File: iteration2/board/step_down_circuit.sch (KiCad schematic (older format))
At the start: 6 parts

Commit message: Redo netlist
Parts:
- C2: renamed from C?; footprint ~ -> Capacitors_SMD:C_0805_HandSoldering
- D1: renamed from D?; footprint ~ -> Diodes_SMD:D_0805
- Q1: renamed from Q?; footprint ~ -> TO_SOT_Packages_SMD:SOT-23
- R1, R2, R3: renamed from R?; footprint ~ -> Resistors_SMD:R_0805_HandSoldering
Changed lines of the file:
@@
 $EndDescr
 $Comp
-L C C?
+L C C2
 U 1 1 59EC7CB5
 P 5200 4500
-F 0 "C?" H 5200 4600 40  0000 L CNN
+AR Path="/59EC784F/59EC7CB5" Ref="C2"  Part="1"
+AR Path="/59EC8586/59EC7CB5" Ref="C3"  Part="1"
+AR Path="/59EC8F0E/59EC7CB5" Ref="C4"  Part="1"
+F 0 "C2" H 5200 4600 40  0000 L CNN
 F 1 "100nF" H 5206 4415 40  0000 L CNN
-F 2 "~" H 5238 4350 30  0000 C CNN
+F 2 "Capacitors_SMD:C_0805_HandSoldering" H 5238 4350 30  0000 C CNN
 F 3 "~" H 5200 4500 60  0000 C CNN
 	1    5200 4500
@@
 $EndComp
 $Comp
-L R R?
+L R R1
 U 1 1 59EC7CBC
 P 5200 4050
-F 0 "R?" V 5280 4050 40  0000 C CNN
+AR Path="/59EC784F/59EC7CBC" Ref="R1"  Part="1"
+AR Path="/59EC8586/59EC7CBC" Ref="R4"  Part="1"
+AR Path="/59EC8F0E/59EC7CBC" Ref="R7"  Part="1"
+F 0 "R1" V 5280 4050 40  0000 C CNN
 F 1 "10K" V 5207 4051 40  0000 C CNN
-F 2 "~" V 5130 4050 30  0000 C CNN
+F 2 "Resistors_SMD:R_0805_HandSoldering" V 5130 4050 30  0000 C CNN
 F 3 "~" H 5200 4050 30  0000 C CNN
 	1    5200 4050
@@
 $EndComp
 $Comp
-L R R?
+L R R2
 U 1 1 59EC7CC3
 P 5450 4300
-F 0 "R?" V 5530 4300 40  0000 C CNN
+AR Path="/59EC784F/59EC7CC3" Ref="R2"  Part="1"
+AR Path="/59EC8586/59EC7CC3" Ref="R5"  Part="1"
+AR Path="/59EC8F0E/59EC7CC3" Ref="R8"  Part="1"
+F 0 "R2" V 5530 4300 40  0000 C CNN
 F 1 "10K" V 5457 4301 40  0000 C CNN
-F 2 "~" V 5380 4300 30  0000 C CNN
+F 2 "Resistors_SMD:R_0805_HandSoldering" V 5380 4300 30  0000 C CNN
 F 3 "~" H 5450 4300 30  0000 C CNN
 	1    5450 4300
@@
 +12V
 $Comp
-L GND #PWR?
+L GND #PWR7
 U 1 1 59EC7CCB
 P 5200 4700
-F 0 "#PWR?" H 5200 4700 30  0001 C CNN
+AR Path="/59EC784F/59EC7CCB" Ref="#PWR7"  Part="1"
+AR Path="/59EC8586/59EC7CCB" Ref="#PWR10"  Part="1"
+AR Path="/59EC8F0E/59EC7CCB" Ref="#PWR13"  Part="1"
+F 0 "#PWR7" H 5200 4700 30  0001 C CNN
 F 1 "GND" H 5200 4630 30  0001 C CNN
 F 2 "" H 5200 4700 60  0000 C CNN
@@
 $EndComp
 $Comp
-L MOS_N Q?
+L MOS_N Q1
 U 1 1 59EC7CD1
 P 6250 4300
-F 0 "Q?" H 6260 4470 60  0000 R CNN
+AR Path="/59EC784F/59EC7CD1" Ref="Q1"  Part="1"
+AR Path="/59EC8586/59EC7CD1" Ref="Q2"  Part="1"
+AR Path="/59EC8F0E/59EC7CD1" Ref="Q3"  Part="1"
+F 0 "Q1" H 6260 4470 60  0000 R CNN
 F 1 "2N7002" H 6260 4150 60  0000 R CNN
-F 2 "~" H 6250 4300 60  0000 C CNN
+F 2 "TO_SOT_Packages_SMD:SOT-23" H 6250 4300 60  0000 C CNN
 F 3 "~" H 6250 4300 60  0000 C CNN
 	1    6250 4300
@@
 $EndComp
 $Comp
-L R R?
+L R R3
 U 1 1 59EC7CD8
 P 6350 3850
-F 0 "R?" V 6430 3850 40  0000 C CNN
+AR Path="/59EC784F/59EC7CD8" Ref="R3"  Part="1"
+AR Path="/59EC8586/59EC7CD8" Ref="R6"  Part="1"
+AR Path="/59EC8F0E/59EC7CD8" Ref="R9"  Part="1"
+F 0 "R3" V 6430 3850 40  0000 C CNN
 F 1 "10K" V 6357 3851 40  0000 C CNN
-F 2 "~" V 6280 3850 30  0000 C CNN
+F 2 "Resistors_SMD:R_0805_HandSoldering" V 6280 3850 30  0000 C CNN
 F 3 "~" H 6350 3850 30  0000 C CNN
 	1    6350 3850
@@
 $EndComp
 $Comp
-L GND #PWR?
+L GND #PWR9
 U 1 1 59EC7CDF
 P 6350 4500
-F 0 "#PWR?" H 6350 4500 30  0001 C CNN
+AR Path="/59EC784F/59EC7CDF" Ref="#PWR9"  Part="1"
+AR Path="/59EC8586/59EC7CDF" Ref="#PWR12"  Part="1"
+AR Path="/59EC8F0E/59EC7CDF" Ref="#PWR15"  Part="1"
+F 0 "#PWR9" H 6350 4500 30  0001 C CNN
 F 1 "GND" H 6350 4430 30  0001 C CNN
 F 2 "" H 6350 4500 60  0000 C CNN
@@
 +3.3V
 $Comp
-L BAV99 D?
+L BAV99 D1
 U 1 1 59EC7CE6
 P 5800 4350
-F 0 "D?" H 5900 4300 40  0000 C CNN
+AR Path="/59EC784F/59EC7CE6" Ref="D1"  Part="1"
+AR Path="/59EC8586/59EC7CE6" Ref="D2"  Part="1"
+AR Path="/59EC8F0E/59EC7CE6" Ref="D3"  Part="1"
+F 0 "D1" H 5900 4300 40  0000 C CNN
 F 1 "BAV99" H 5900 4400 40  0001 C CNN
-F 2 "~" V 5850 4300 60  0000 C CNN
+F 2 "Diodes_SMD:D_0805" V 5850 4300 60  0000 C CNN
 F 3 "~" V 5850 4300 60  0000 C CNN
 	1    5800 4350
@@
 	5700 4600 5700 4300
 $Comp
-L GND #PWR?
+L GND #PWR8
 U 1 1 59EC7CF0
 P 5800 4500
-F 0 "#PWR?" H 5800 4500 30  0001 C CNN
+AR Path="/59EC784F/59EC7CF0" Ref="#PWR8"  Part="1"
+AR Path="/59EC8586/59EC7CF0" Ref="#PWR11"  Part="1"
+AR Path="/59EC8F0E/59EC7CF0" Ref="#PWR14"  Part="1"
+F 0 "#PWR8" H 5800 4500 30  0001 C CNN
 F 1 "GND" H 5800 4430 30  0001 C CNN
 F 2 "" H 5800 4500 60  0000 C CNN

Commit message: Generated netlist
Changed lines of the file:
@@
 AR Path="/59EC8586/59EC7CB5" Ref="C3"  Part="1"
 AR Path="/59EC8F0E/59EC7CB5" Ref="C4"  Part="1"
-F 0 "C2" H 5200 4600 40  0000 L CNN
+F 0 "C4" H 5200 4600 40  0000 L CNN
 F 1 "100nF" H 5206 4415 40  0000 L CNN
 F 2 "Capacitors_SMD:C_0805_HandSoldering" H 5238 4350 30  0000 C CNN
@@
 AR Path="/59EC8586/59EC7CBC" Ref="R4"  Part="1"
 AR Path="/59EC8F0E/59EC7CBC" Ref="R7"  Part="1"
-F 0 "R1" V 5280 4050 40  0000 C CNN
+F 0 "R7" V 5280 4050 40  0000 C CNN
 F 1 "10K" V 5207 4051 40  0000 C CNN
 F 2 "Resistors_SMD:R_0805_HandSoldering" V 5130 4050 30  0000 C CNN
@@
 AR Path="/59EC8586/59EC7CC3" Ref="R5"  Part="1"
 AR Path="/59EC8F0E/59EC7CC3" Ref="R8"  Part="1"
-F 0 "R2" V 5530 4300 40  0000 C CNN
+F 0 "R8" V 5530 4300 40  0000 C CNN
 F 1 "10K" V 5457 4301 40  0000 C CNN
 F 2 "Resistors_SMD:R_0805_HandSoldering" V 5380 4300 30  0000 C CNN
@@
 AR Path="/59EC8586/59EC7CD1" Ref="Q2"  Part="1"
 AR Path="/59EC8F0E/59EC7CD1" Ref="Q3"  Part="1"
-F 0 "Q1" H 6260 4470 60  0000 R CNN
+F 0 "Q3" H 6260 4470 60  0000 R CNN
 F 1 "2N7002" H 6260 4150 60  0000 R CNN
 F 2 "TO_SOT_Packages_SMD:SOT-23" H 6250 4300 60  0000 C CNN
@@
 AR Path="/59EC8586/59EC7CD8" Ref="R6"  Part="1"
 AR Path="/59EC8F0E/59EC7CD8" Ref="R9"  Part="1"
-F 0 "R3" V 6430 3850 40  0000 C CNN
+F 0 "R9" V 6430 3850 40  0000 C CNN
 F 1 "10K" V 6357 3851 40  0000 C CNN
 F 2 "Resistors_SMD:R_0805_HandSoldering" V 6280 3850 30  0000 C CNN
@@
 AR Path="/59EC8586/59EC7CE6" Ref="D2"  Part="1"
 AR Path="/59EC8F0E/59EC7CE6" Ref="D3"  Part="1"
-F 0 "D1" H 5900 4300 40  0000 C CNN
+F 0 "D3" H 5900 4300 40  0000 C CNN
 F 1 "BAV99" H 5900 4400 40  0001 C CNN
 F 2 "Diodes_SMD:D_0805" V 5850 4300 60  0000 C CNN

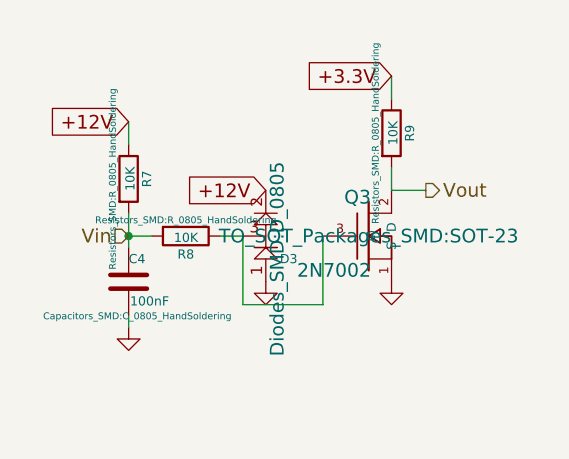
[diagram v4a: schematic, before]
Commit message: Redid some components to fit footprint
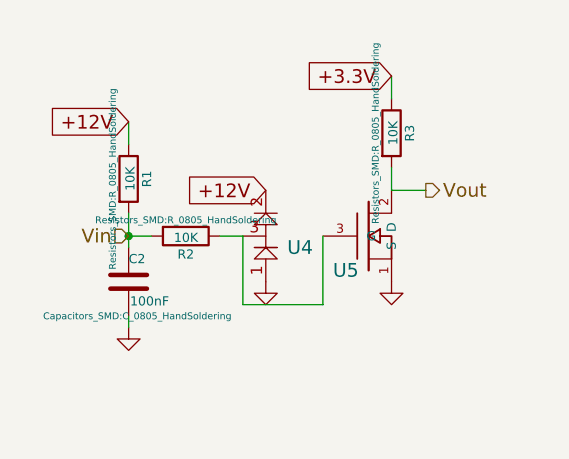
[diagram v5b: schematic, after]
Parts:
- removed D1: BAV99, Diodes_SMD:D_0805, symbol BAV99
- removed Q1: 2N7002, TO_SOT_Packages_SMD:SOT-23, symbol MOS_N
- added U7: MOS_N, TO_SOT_Packages_SMD:SOT-23, symbol MOS_N
- added U8: BAV99, TO_SOT_Packages_SMD:SOT-23, symbol BAV99
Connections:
- net +12V: now also U8.2
- net GND: now also U7.1 (S), U8.1
- net Vout: now also U7.2 (D)
- net at R2.1: now also U7.3 (G), U8.3
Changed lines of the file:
@@
 $Descr A4 11693 8268
 encoding utf-8
-Sheet 2 5
+Sheet 3 5
 Title ""
 Date ""
@@
 AR Path="/59EC8586/59EC7CB5" Ref="C3"  Part="1"
 AR Path="/59EC8F0E/59EC7CB5" Ref="C4"  Part="1"
-F 0 "C4" H 5200 4600 40  0000 L CNN
+F 0 "C2" H 5200 4600 40  0000 L CNN
 F 1 "100nF" H 5206 4415 40  0000 L CNN
 F 2 "Capacitors_SMD:C_0805_HandSoldering" H 5238 4350 30  0000 C CNN
@@
 AR Path="/59EC8586/59EC7CBC" Ref="R4"  Part="1"
 AR Path="/59EC8F0E/59EC7CBC" Ref="R7"  Part="1"
-F 0 "R7" V 5280 4050 40  0000 C CNN
+F 0 "R1" V 5280 4050 40  0000 C CNN
 F 1 "10K" V 5207 4051 40  0000 C CNN
 F 2 "Resistors_SMD:R_0805_HandSoldering" V 5130 4050 30  0000 C CNN
@@
 AR Path="/59EC8586/59EC7CC3" Ref="R5"  Part="1"
 AR Path="/59EC8F0E/59EC7CC3" Ref="R8"  Part="1"
-F 0 "R8" V 5530 4300 40  0000 C CNN
+F 0 "R2" V 5530 4300 40  0000 C CNN
 F 1 "10K" V 5457 4301 40  0000 C CNN
 F 2 "Resistors_SMD:R_0805_HandSoldering" V 5380 4300 30  0000 C CNN
@@
 $EndComp
 $Comp
-L MOS_N Q1
-U 1 1 59EC7CD1
-P 6250 4300
-AR Path="/59EC784F/59EC7CD1" Ref="Q1"  Part="1"
-AR Path="/59EC8586/59EC7CD1" Ref="Q2"  Part="1"
-AR Path="/59EC8F0E/59EC7CD1" Ref="Q3"  Part="1"
-F 0 "Q3" H 6260 4470 60  0000 R CNN
-F 1 "2N7002" H 6260 4150 60  0000 R CNN
-F 2 "TO_SOT_Packages_SMD:SOT-23" H 6250 4300 60  0000 C CNN
-F 3 "~" H 6250 4300 60  0000 C CNN
-	1    6250 4300
-	1    0    0    -1
-$EndComp
-$Comp
 L R R3
 U 1 1 59EC7CD8
@@
 AR Path="/59EC8586/59EC7CD8" Ref="R6"  Part="1"
 AR Path="/59EC8F0E/59EC7CD8" Ref="R9"  Part="1"
-F 0 "R9" V 6430 3850 40  0000 C CNN
+F 0 "R3" V 6430 3850 40  0000 C CNN
 F 1 "10K" V 6357 3851 40  0000 C CNN
 F 2 "Resistors_SMD:R_0805_HandSoldering" V 6280 3850 30  0000 C CNN
@@
 Text GLabel 6350 3600 0    60   Input ~ 0
 +3.3V
-$Comp
-L BAV99 D1
-U 1 1 59EC7CE6
-P 5800 4350
-AR Path="/59EC784F/59EC7CE6" Ref="D1"  Part="1"
-AR Path="/59EC8586/59EC7CE6" Ref="D2"  Part="1"
-AR Path="/59EC8F0E/59EC7CE6" Ref="D3"  Part="1"
-F 0 "D3" H 5900 4300 40  0000 C CNN
-F 1 "BAV99" H 5900 4400 40  0001 C CNN
-F 2 "Diodes_SMD:D_0805" V 5850 4300 60  0000 C CNN
-F 3 "~" V 5850 4300 60  0000 C CNN
-	1    5800 4350
-	1    0    0    -1
-$EndComp
 Wire Wire Line
 	6050 4300 6050 4600
@@
 Text HLabel 6500 4100 2    60   Output ~ 0
 Vout
+$Comp
+L BAV99 U8
+U 1 1 59F295CD
+P 5800 4350
+AR Path="/59EC8F0E/59F295CD" Ref="U8"  Part="1"
+AR Path="/59EC8586/59F295CD" Ref="U6"  Part="1"
+AR Path="/59EC784F/59F295CD" Ref="U4"  Part="1"
+F 0 "U4" H 5950 4350 60  0000 C CNN
+F 1 "BAV99" H 6050 4450 60  0001 C CNN
+F 2 "TO_SOT_Packages_SMD:SOT-23" H 5800 4350 60  0001 C CNN
+F 3 "" H 5800 4350 60  0001 C CNN
+	1    5800 4350
+	1    0    0    -1
+$EndComp
+$Comp
+L MOS_N U7
+U 1 1 59F29BA9
+P 6250 4300
+AR Path="/59EC8586/59F29BA9" Ref="U7"  Part="1"
+AR Path="/59EC784F/59F29BA9" Ref="U5"  Part="1"
+AR Path="/59EC8F0E/59F29BA9" Ref="U9"  Part="1"
+F 0 "U5" H 6150 4150 60  0000 C CNN
+F 1 "MOS_N" H 6550 4350 60  0001 C CNN
+F 2 "TO_SOT_Packages_SMD:SOT-23" H 6250 4300 60  0001 C CNN
+F 3 "" H 6250 4300 60  0001 C CNN
+	1    6250 4300
+	1    0    0    -1
+$EndComp
 $EndSCHEMATC

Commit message: partially resolved merge issues and added script for automatic merging
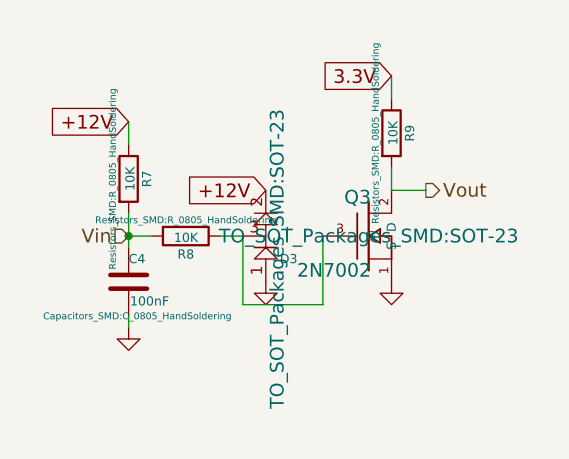
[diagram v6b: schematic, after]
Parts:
- removed U7: MOS_N, TO_SOT_Packages_SMD:SOT-23, symbol MOS_N
- removed U8: BAV99, TO_SOT_Packages_SMD:SOT-23, symbol BAV99
- added D2: BAV99, TO_SOT_Packages_SMD:SOT-23, symbol BAV99
- added Q2: 2N7002, TO_SOT_Packages_SMD:SOT-23, symbol MOS_N
- renumbered C2 to C3, R1 to R4, R2 to R5, R3 to R6
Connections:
- net +12V: now also D2.2
- net GND: now also D2.1, Q2.1 (S)
- net Vout: now also Q2.2 (D)
- net at R5.1: now also D2.3, Q2.3 (G)
- net +3.3V renamed 3.3V
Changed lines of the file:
@@
 $Descr A4 11693 8268
 encoding utf-8
-Sheet 3 5
+Sheet 4 5
 Title ""
 Date ""
@@
 $EndDescr
 $Comp
-L C C2
+L C C3
 U 1 1 59EC7CB5
 P 5200 4500
-AR Path="/59EC784F/59EC7CB5" Ref="C2"  Part="1"
 AR Path="/59EC8586/59EC7CB5" Ref="C3"  Part="1"
 AR Path="/59EC8F0E/59EC7CB5" Ref="C4"  Part="1"
-F 0 "C2" H 5200 4600 40  0000 L CNN
+AR Path="/59EC784F/59EC7CB5" Ref="C2"  Part="1"
+F 0 "C4" H 5200 4600 40  0000 L CNN
 F 1 "100nF" H 5206 4415 40  0000 L CNN
 F 2 "Capacitors_SMD:C_0805_HandSoldering" H 5238 4350 30  0000 C CNN
@@
 $EndComp
 $Comp
-L R R1
+L R R4
 U 1 1 59EC7CBC
 P 5200 4050
-AR Path="/59EC784F/59EC7CBC" Ref="R1"  Part="1"
 AR Path="/59EC8586/59EC7CBC" Ref="R4"  Part="1"
 AR Path="/59EC8F0E/59EC7CBC" Ref="R7"  Part="1"
-F 0 "R1" V 5280 4050 40  0000 C CNN
+AR Path="/59EC784F/59EC7CBC" Ref="R1"  Part="1"
+F 0 "R7" V 5280 4050 40  0000 C CNN
 F 1 "10K" V 5207 4051 40  0000 C CNN
 F 2 "Resistors_SMD:R_0805_HandSoldering" V 5130 4050 30  0000 C CNN
@@
 $EndComp
 $Comp
-L R R2
+L R R5
 U 1 1 59EC7CC3
 P 5450 4300
-AR Path="/59EC784F/59EC7CC3" Ref="R2"  Part="1"
 AR Path="/59EC8586/59EC7CC3" Ref="R5"  Part="1"
 AR Path="/59EC8F0E/59EC7CC3" Ref="R8"  Part="1"
-F 0 "R2" V 5530 4300 40  0000 C CNN
+AR Path="/59EC784F/59EC7CC3" Ref="R2"  Part="1"
+F 0 "R8" V 5530 4300 40  0000 C CNN
 F 1 "10K" V 5457 4301 40  0000 C CNN
 F 2 "Resistors_SMD:R_0805_HandSoldering" V 5380 4300 30  0000 C CNN
@@
 +12V
 $Comp
-L GND #PWR07
+L GND #PWR10
 U 1 1 59EC7CCB
 P 5200 4700
-AR Path="/59EC784F/59EC7CCB" Ref="#PWR07"  Part="1"
-AR Path="/59EC8586/59EC7CCB" Ref="#PWR010"  Part="1"
-AR Path="/59EC8F0E/59EC7CCB" Ref="#PWR013"  Part="1"
-F 0 "#PWR013" H 5200 4700 30  0001 C CNN
+AR Path="/59EC8586/59EC7CCB" Ref="#PWR10"  Part="1"
+AR Path="/59EC8F0E/59EC7CCB" Ref="#PWR13"  Part="1"
+AR Path="/59EC784F/59EC7CCB" Ref="#PWR7"  Part="1"
+F 0 "#PWR13" H 5200 4700 30  0001 C CNN
 F 1 "GND" H 5200 4630 30  0001 C CNN
 F 2 "" H 5200 4700 60  0000 C CNN
@@
 $EndComp
 $Comp
-L R R3
+L MOS_N Q2
+U 1 1 59EC7CD1
+P 6250 4300
+AR Path="/59EC8586/59EC7CD1" Ref="Q2"  Part="1"
+AR Path="/59EC8F0E/59EC7CD1" Ref="Q3"  Part="1"
+AR Path="/59EC784F/59EC7CD1" Ref="Q1"  Part="1"
+F 0 "Q3" H 6260 4470 60  0000 R CNN
+F 1 "2N7002" H 6260 4150 60  0000 R CNN
+F 2 "TO_SOT_Packages_SMD:SOT-23" H 6250 4300 60  0000 C CNN
+F 3 "~" H 6250 4300 60  0000 C CNN
+	1    6250 4300
+	1    0    0    -1
+$EndComp
+$Comp
+L R R6
 U 1 1 59EC7CD8
 P 6350 3850
-AR Path="/59EC784F/59EC7CD8" Ref="R3"  Part="1"
 AR Path="/59EC8586/59EC7CD8" Ref="R6"  Part="1"
 AR Path="/59EC8F0E/59EC7CD8" Ref="R9"  Part="1"
-F 0 "R3" V 6430 3850 40  0000 C CNN
+AR Path="/59EC784F/59EC7CD8" Ref="R3"  Part="1"
+F 0 "R9" V 6430 3850 40  0000 C CNN
 F 1 "10K" V 6357 3851 40  0000 C CNN
 F 2 "Resistors_SMD:R_0805_HandSoldering" V 6280 3850 30  0000 C CNN
@@
 $EndComp
 $Comp
-L GND #PWR08
+L GND #PWR12
 U 1 1 59EC7CDF
 P 6350 4500
-AR Path="/59EC784F/59EC7CDF" Ref="#PWR08"  Part="1"
-AR Path="/59EC8586/59EC7CDF" Ref="#PWR011"  Part="1"
-AR Path="/59EC8F0E/59EC7CDF" Ref="#PWR014"  Part="1"
-F 0 "#PWR014" H 6350 4500 30  0001 C CNN
+AR Path="/59EC8586/59EC7CDF" Ref="#PWR12"  Part="1"
+AR Path="/59EC8F0E/59EC7CDF" Ref="#PWR15"  Part="1"
+AR Path="/59EC784F/59EC7CDF" Ref="#PWR9"  Part="1"
+F 0 "#PWR15" H 6350 4500 30  0001 C CNN
 F 1 "GND" H 6350 4430 30  0001 C CNN
 F 2 "" H 6350 4500 60  0000 C CNN
@@
 	1    0    0    -1
 $EndComp
-Text GLabel 6350 3600 0    60   Input ~ 0
-+3.3V
+$Comp
+L BAV99 D2
+U 1 1 59EC7CE6
+P 5800 4350
+AR Path="/59EC8586/59EC7CE6" Ref="D2"  Part="1"
+AR Path="/59EC8F0E/59EC7CE6" Ref="D3"  Part="1"
+AR Path="/59EC784F/59EC7CE6" Ref="D1"  Part="1"
+F 0 "D3" H 5900 4300 40  0000 C CNN
+F 1 "BAV99" H 5900 4400 40  0001 C CNN
+F 2 "TO_SOT_Packages_SMD:SOT-23" V 5850 4300 60  0000 C CNN
+F 3 "~" V 5850 4300 60  0000 C CNN
+	1    5800 4350
+	1    0    0    -1
+$EndComp
 Wire Wire Line
 	6050 4300 6050 4600
@@
 	5700 4600 5700 4300
 $Comp
-L GND #PWR09
+L GND #PWR11
 U 1 1 59EC7CF0
 P 5800 4500
-AR Path="/59EC784F/59EC7CF0" Ref="#PWR09"  Part="1"
-AR Path="/59EC8586/59EC7CF0" Ref="#PWR012"  Part="1"
-AR Path="/59EC8F0E/59EC7CF0" Ref="#PWR015"  Part="1"
-F 0 "#PWR015" H 5800 4500 30  0001 C CNN
+AR Path="/59EC8586/59EC7CF0" Ref="#PWR11"  Part="1"
+AR Path="/59EC8F0E/59EC7CF0" Ref="#PWR14"  Part="1"
+AR Path="/59EC784F/59EC7CF0" Ref="#PWR8"  Part="1"
+F 0 "#PWR14" H 5800 4500 30  0001 C CNN
 F 1 "GND" H 5800 4430 30  0001 C CNN
 F 2 "" H 5800 4500 60  0000 C CNN
@@
 Text HLabel 6500 4100 2    60   Output ~ 0
 Vout
-$Comp
-L BAV99 U8
-U 1 1 59F295CD
-P 5800 4350
-AR Path="/59EC8F0E/59F295CD" Ref="U8"  Part="1"
-AR Path="/59EC8586/59F295CD" Ref="U6"  Part="1"
-AR Path="/59EC784F/59F295CD" Ref="U4"  Part="1"
-F 0 "U4" H 5950 4350 60  0000 C CNN
-F 1 "BAV99" H 6050 4450 60  0001 C CNN
-F 2 "TO_SOT_Packages_SMD:SOT-23" H 5800 4350 60  0001 C CNN
-F 3 "" H 5800 4350 60  0001 C CNN
-	1    5800 4350
-	1    0    0    -1
-$EndComp
-$Comp
-L MOS_N U7
-U 1 1 59F29BA9
-P 6250 4300
-AR Path="/59EC8586/59F29BA9" Ref="U7"  Part="1"
-AR Path="/59EC784F/59F29BA9" Ref="U5"  Part="1"
-AR Path="/59EC8F0E/59F29BA9" Ref="U9"  Part="1"
-F 0 "U5" H 6150 4150 60  0000 C CNN
-F 1 "MOS_N" H 6550 4350 60  0001 C CNN
-F 2 "TO_SOT_Packages_SMD:SOT-23" H 6250 4300 60  0001 C CNN
-F 3 "" H 6250 4300 60  0001 C CNN
-	1    6250 4300
-	1    0    0    -1
-$EndComp
+Text GLabel 6350 3600 0    60   Input ~ 0
+3.3V
 $EndSCHEMATC
